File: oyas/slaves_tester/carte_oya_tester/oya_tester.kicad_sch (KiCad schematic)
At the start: 55 parts, among them J1 Power, J2 Bus Oya, J6 Switches, SW3 Address, SW4 Select, U1 D148K, U2 MAX485E, U3 BPC_Alim5V, X2 Trou, X3 Trou, X4 Trou

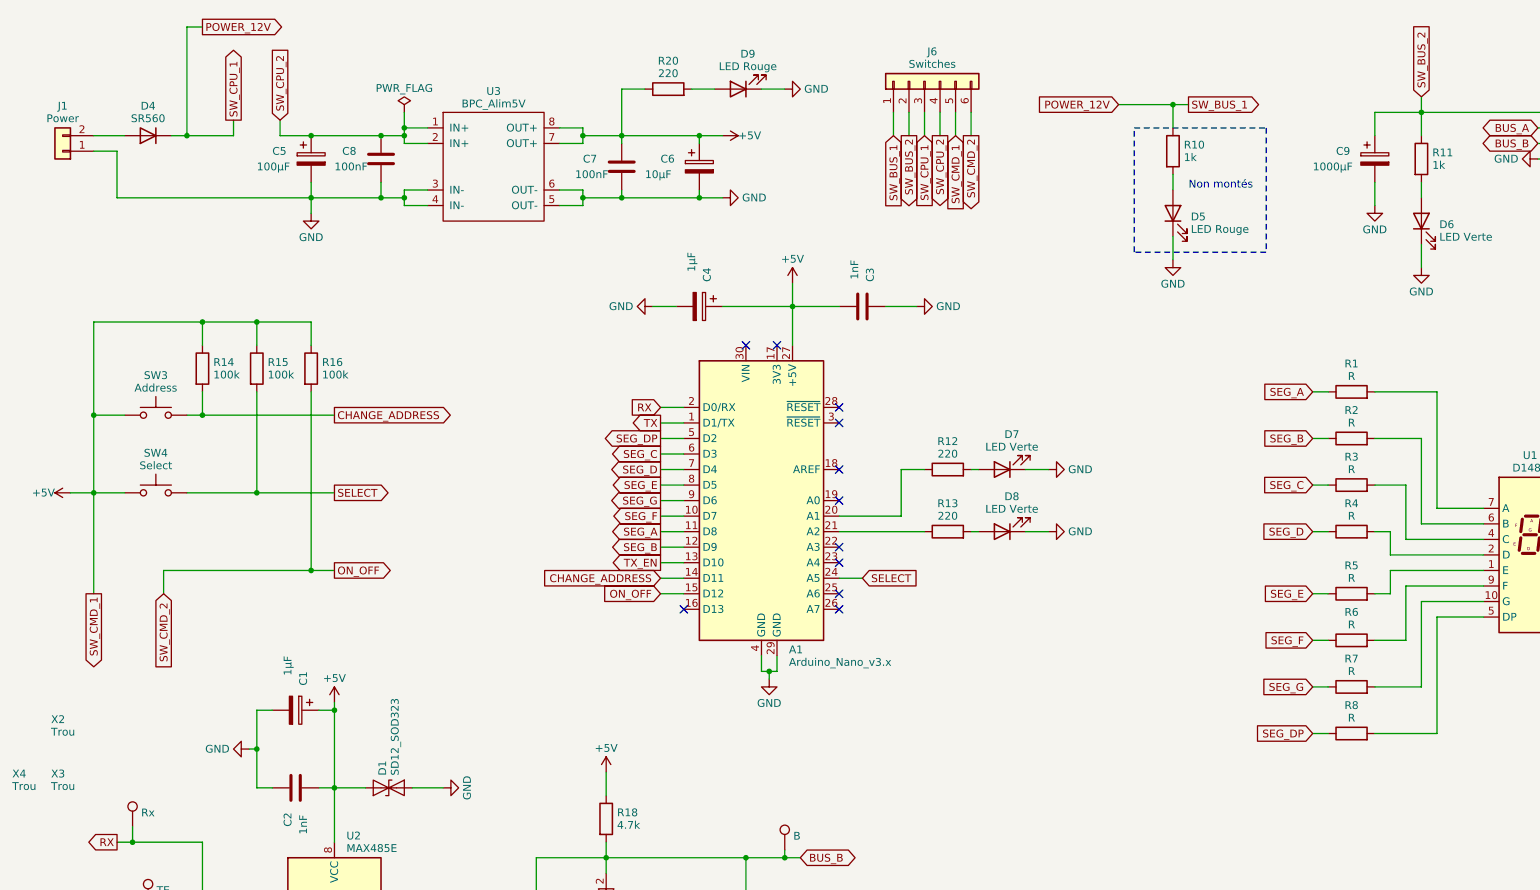
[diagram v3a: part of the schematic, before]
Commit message: Réception rev A et corrections: - Les SW étaient à 5V au lieu de GND - Idem sur le connecteur JST du SW ON/OFF - Valeur des résistances anodes du 7seg à 220 Ohms
Passage en Rev B pour la suivante

+ Ajout su soft de départ
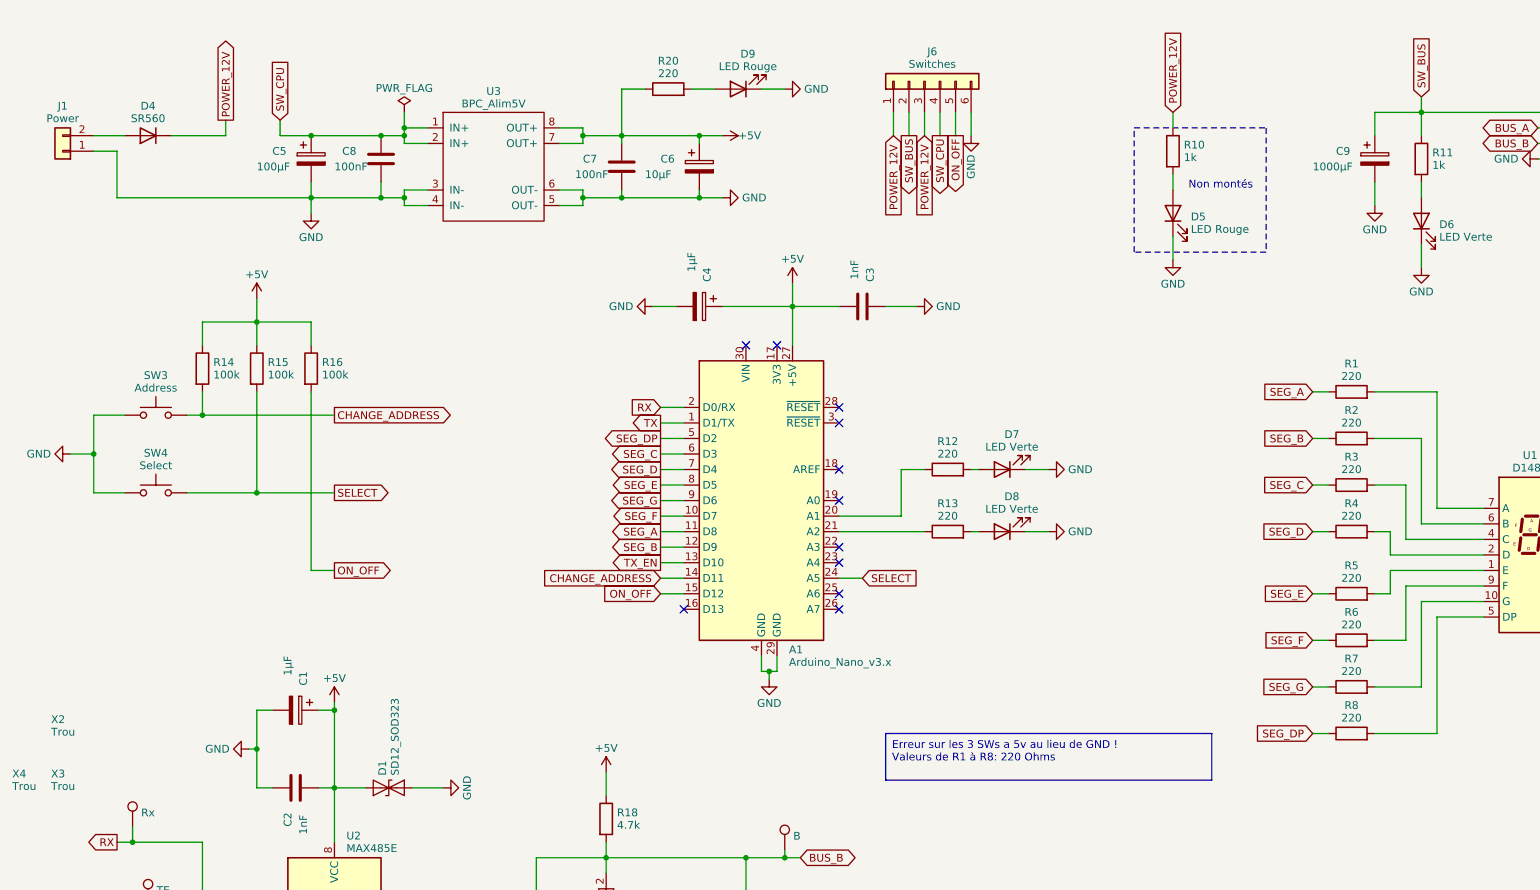
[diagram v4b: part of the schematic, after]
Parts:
- R1, R2, R3, R4, R5, R6, R7, R8: value R -> 220
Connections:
- net +5V: no longer J6.5 (Pin_5), SW3.1, SW4.1
- net GND: now also J6.6 (Pin_6), SW3.1, SW4.1
- net ON_OFF: now also J6.5 (Pin_5); no longer J6.6 (Pin_6)
- net SW_BUS_2 renamed SW_BUS
- net SW_CPU_2 renamed SW_CPU

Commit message: .
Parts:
- D1, D3: footprint Diode_SMD:D_SOD-323 -> bpc:BPC_D_SOD-323_HandSoldering; symbol Diode:SD12_SOD323 -> bpc:BPC_SD12_SOD323
- D2: value SM712_SOT23 -> BPC_SM712_SOT23; footprint Package_TO_SOT_SMD:SOT-23 -> bpc:BPC_SOT-23-3_HandSoldering; symbol Diode:SM712_SOT23 -> bpc:BPC_SM712_SOT23
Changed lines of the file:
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@@
     (fill (type none))
   )
-  (text_box "Erreur sur les 3 SWs a 5v au lieu de GND !\nValeurs de R1 à R8: 220 Ohms"
-    (at 158.75 134.62 0) (size 53.34 7.62)
+  (text_box "Corrections Rev B:\n\nErreur sur les 3 SWs a 5v au lieu de GND !\nValeurs de R1 à R8: 220 Ohms\nEmpreintes D1, D2 et D3 / hand solder"
+    (at 158.75 134.62 0) (size 53.34 13.97)
     (stroke (width 0) (type default))
     (fill (type none))
@@
   )
   (symbol (lib_id "bpc:BPC_MAX485E") (at 68.58 165.1 0) (unit 1)
-    (in_bom yes) (on_board yes) (dnp no) (fields_autoplaced)
-    (property "Reference" "U2" (at 70.5359 151.36 0)
-      (effects (font (size 1.27 1.27)) (justify left))
-    )
-    (property "Value" "MAX485E" (at 70.5359 153.408 0)
+    (in_bom yes) (on_board yes) (dnp no)
+    (property "Reference" "U2" (at 71.12 149.86 0)
+      (effects (font (size 1.27 1.27)) (justify left))
+    )
+    (property "Value" "MAX485E" (at 71.12 152.4 0)
       (effects (font (size 1.27 1.27)) (justify left))
     )
@@
       (effects (font (size 1.27 1.27)) hide)
     )
-    (property "Fabricant" "Analog Devices" (at 68.58 165.1 0)
-      (effects (font (size 1.27 1.27)) hide)
-    )
-    (property "Fournisseur" "Farnell" (at 68.58 165.1 0)
-      (effects (font (size 1.27 1.27)) hide)
-    )
-    (property "RefFabricant" "MAX485ESA+" (at 68.58 165.1 0)
-      (effects (font (size 1.27 1.27)) hide)
-    )
-    (property "RefFournisseur" "2519382" (at 68.58 165.1 0)
-      (effects (font (size 1.27 1.27)) hide)
+    (property "Fabricant" "Analog Devices" (at 70.5359 147.264 0)
+      (effects (font (size 1.27 1.27)) (justify left) hide)
+    )
+    (property "Fournisseur" "Farnell" (at 70.5359 149.312 0)
+      (effects (font (size 1.27 1.27)) (justify left) hide)
+    )
+    (property "RefFabricant" "MAX485ESA+" (at 70.5359 151.36 0)
+      (effects (font (size 1.27 1.27)) (justify left) hide)
+    )
+    (property "RefFournisseur" "2519382" (at 70.5359 153.408 0)
+      (effects (font (size 1.27 1.27)) (justify left) hide)
     )
     (pin "1")
@@
     )
   )
-  (symbol (lib_id "Diode:SM712_SOT23") (at 113.03 166.37 90) (unit 1)
-    (in_bom yes) (on_board yes) (dnp no) (fields_autoplaced)
-    (property "Reference" "D2" (at 111.0234 165.346 90)
-      (effects (font (size 1.27 1.27)) (justify left))
-    )
-    (property "Value" "SM712_SOT23" (at 111.0234 167.394 90)
-      (effects (font (size 1.27 1.27)) (justify left))
-    )
-    (property "Footprint" "Package_TO_SOT_SMD:SOT-23" (at 121.92 166.37 0)
-      (effects (font (size 1.27 1.27)) hide)
-    )
-    (property "Datasheet" "https://www.littelfuse.com/~/media/electronics/datasheets/tvs_diode_arrays/littelfuse_tvs_diode_array_sm712_datasheet.pdf.pdf" (at 113.03 170.18 0)
+  (symbol (lib_id "bpc:BPC_SM712_SOT23") (at 113.03 166.37 90) (unit 1)
+    (in_bom yes) (on_board yes) (dnp no)
+    (property "Reference" "D2" (at 107.95 166.37 90)
+      (effects (font (size 1.27 1.27)) (justify left))
+    )
+    (property "Value" "BPC_SM712_SOT23" (at 109.22 166.37 0)
+      (effects (font (size 1.27 1.27)))
+    )
+    (property "Footprint" "bpc:BPC_SOT-23-3_HandSoldering" (at 124.46 166.37 0)
+      (effects (font (size 1.27 1.27)) hide)
+    )
+    (property "Datasheet" "https://www.littelfuse.com/~/media/electronics/datasheets/tvs_diode_arrays/littelfuse_tvs_diode_array_sm712_datasheet.pdf.pdf" (at 128.27 163.83 0)
       (effects (font (size 1.27 1.27)) hide)
     )
@@
     )
   )
-  (symbol (lib_id "Diode:SD12_SOD323") (at 135.89 165.1 90) (unit 1)
+  (symbol (lib_id "bpc:BPC_SD12_SOD323") (at 135.89 165.1 90) (unit 1)
     (in_bom yes) (on_board yes) (dnp no) (fields_autoplaced)
     (property "Reference" "D3" (at 137.8966 164.076 90)
@@
       (effects (font (size 1.27 1.27)) (justify right))
     )
-    (property "Footprint" "Diode_SMD:D_SOD-323" (at 140.97 165.1 0)
+    (property "Footprint" "bpc:BPC_D_SOD-323_HandSoldering" (at 140.97 165.1 0)
       (effects (font (size 1.27 1.27)) hide)
     )
@@
     )
   )
-  (symbol (lib_id "Diode:SD12_SOD323") (at 77.47 143.51 0) (unit 1)
+  (symbol (lib_id "bpc:BPC_SD12_SOD323") (at 77.47 143.51 0) (unit 1)
     (in_bom yes) (on_board yes) (dnp no) (fields_autoplaced)
     (property "Reference" "D1" (at 76.446 141.5034 90)
@@
       (effects (font (size 1.27 1.27)) (justify left))
     )
-    (property "Footprint" "Diode_SMD:D_SOD-323" (at 77.47 148.59 0)
-      (effects (font (size 1.27 1.27)) hide)
-    )
+    (property "Footprint" "bpc:BPC_D_SOD-323_HandSoldering" (at 77.47 148.59 0)
+      (effects (font (size 1.27 1.27)) hide)
+    )

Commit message: Préparation carte future Rev B (Correction SW) Mise au point programme.
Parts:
- added D10: LED Rouge, LED_THT:LED_D3.0mm_FlatTop, symbol Device:LED
- added D11: 1V4007, Diode_THT:D_DO-41_SOD81_P10.16mm_Horizontal, symbol Device:D
- added D12, D13: P6KE16A, Diode_THT:D_DO-15_P10.16mm_Horizontal, symbol bpc:BPC_SD12_SOD323
- added J3: EV, TerminalBlock_Phoenix:TerminalBlock_Phoenix_MKDS-1,5-2-5.08_1x02_P5.08mm_Horizontal, symbol Connector_Generic:Conn_01x02
- added R21: 1k, Resistor_SMD:R_0805_2012Metric_Pad1.20x1.40mm_HandSolder, symbol Device:R
- J6: symbol Connector_Generic:Conn_01x06 -> Connector_Generic:Conn_01x08; Type (none) -> Embase JST VH3.96mm
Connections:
- net GND: now also D10.1 (K), D11.2 (A), D12.1 (A1), D13.1 (A1), J3.2 (Pin_2)
- net POWER_12V: now also J6.7 (Pin_7), D13.2 (A2)
- new net: D10.2 (A), R21.2
- new net SW_TST_EV2: D11.1 (K), D12.2 (A2), J3.1 (Pin_1), J6.8 (Pin_8), R21.1
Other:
- note added: "Mettre une TVS à l'entrée sur le 12V (cf projet oya M0) Ajouter une sortie de test EV avec diode de roue libre + Connextion BP extérieur + LED (circuit séparé)"
- moved on the sheet: A1, C3, C4, D7, D8, R12, R13

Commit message: Finalisation future Rev B
Ajout de protections sur le 12V Bus
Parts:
- added D14: 1N4007, Diode_THT:D_DO-41_SOD81_P3.81mm_Vertical_KathodeUp, symbol Device:D
- added D15: P6KE16A, Diode_THT:D_DO-15_P3.81mm_Vertical_KathodeUp, symbol bpc:BPC_SD12_SOD323
- D11: value 1V4007 -> 1N4007; footprint Diode_THT:D_DO-41_SOD81_P10.16mm_Horizontal -> Diode_THT:D_DO-41_SOD81_P3.81mm_Vertical_KathodeUp
- D12: footprint Diode_THT:D_DO-15_P10.16mm_Horizontal -> Diode_THT:D_DO-15_P3.81mm_Vertical_KathodeUp
- J6: footprint Connector_JST:JST_VH_B6P-VH-FB-B_1x06_P3.96mm_Vertical -> Connector_JST:JST_VH_B8P-VH-B_1x08_P3.96mm_Vertical
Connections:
- net GND: now also J6.8 (Pin_8), D14.2 (A), D15.1 (A1); no longer J6.6 (Pin_6)
- net ON_OFF: now also J6.7 (Pin_7); no longer J6.5 (Pin_5)
- net POWER_12V: now also C9.1, J6.5 (Pin_5); no longer J6.7 (Pin_7)
- net SW_BUS: now also J6.4 (Pin_4), D14.1 (K), D15.2 (A2); no longer C9.1, J6.2 (Pin_2)
- net SW_CPU: now also J6.6 (Pin_6); no longer J6.4 (Pin_4)
- net SW_TST_EV2 renamed SW_TST_EV
- net SW_TST_EV: now also J6.2 (Pin_2); no longer J6.8 (Pin_8)
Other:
- note removed: "Mettre une TVS à l'entrée sur le 12V (cf projet oya M0) Ajouter une sortie de test EV avec diode de roue libre + Connextion BP extérieur + LED (circuit séparé)"
- moved on the sheet: C5, C8, C9, D11, D12, D13, D4, D5, R10
